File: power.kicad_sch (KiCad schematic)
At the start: 33 parts, among them U5 TI LMR54410DBV, U6 INA3221AIRGV

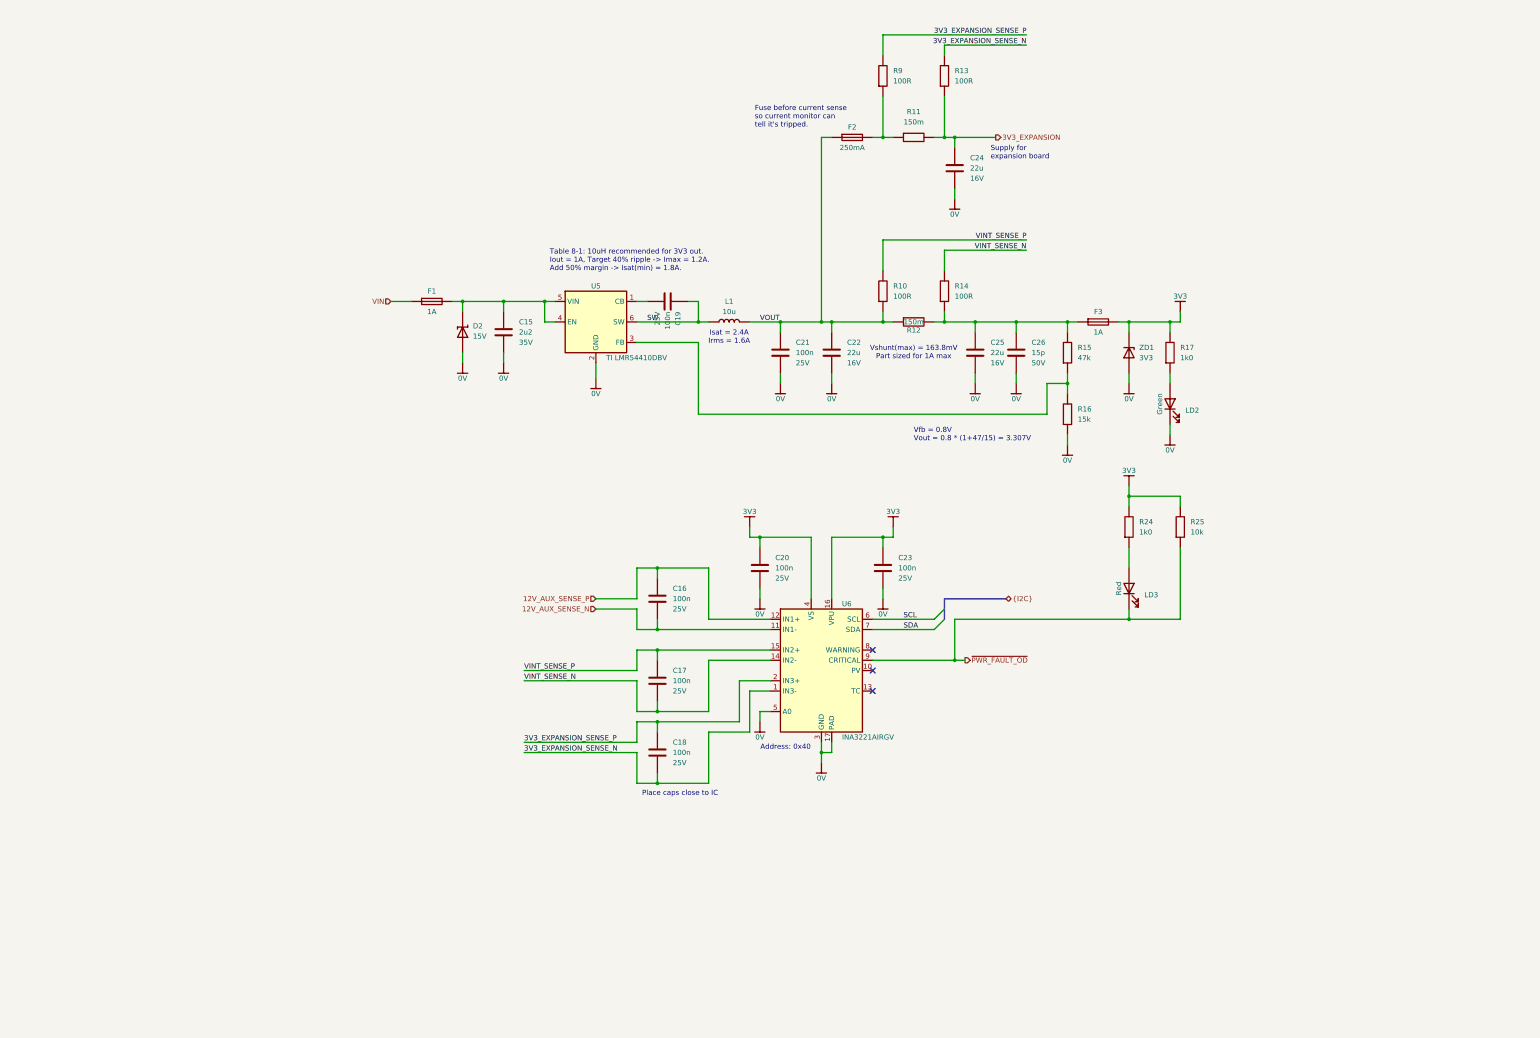
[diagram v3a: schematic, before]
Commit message: added 5v regulator
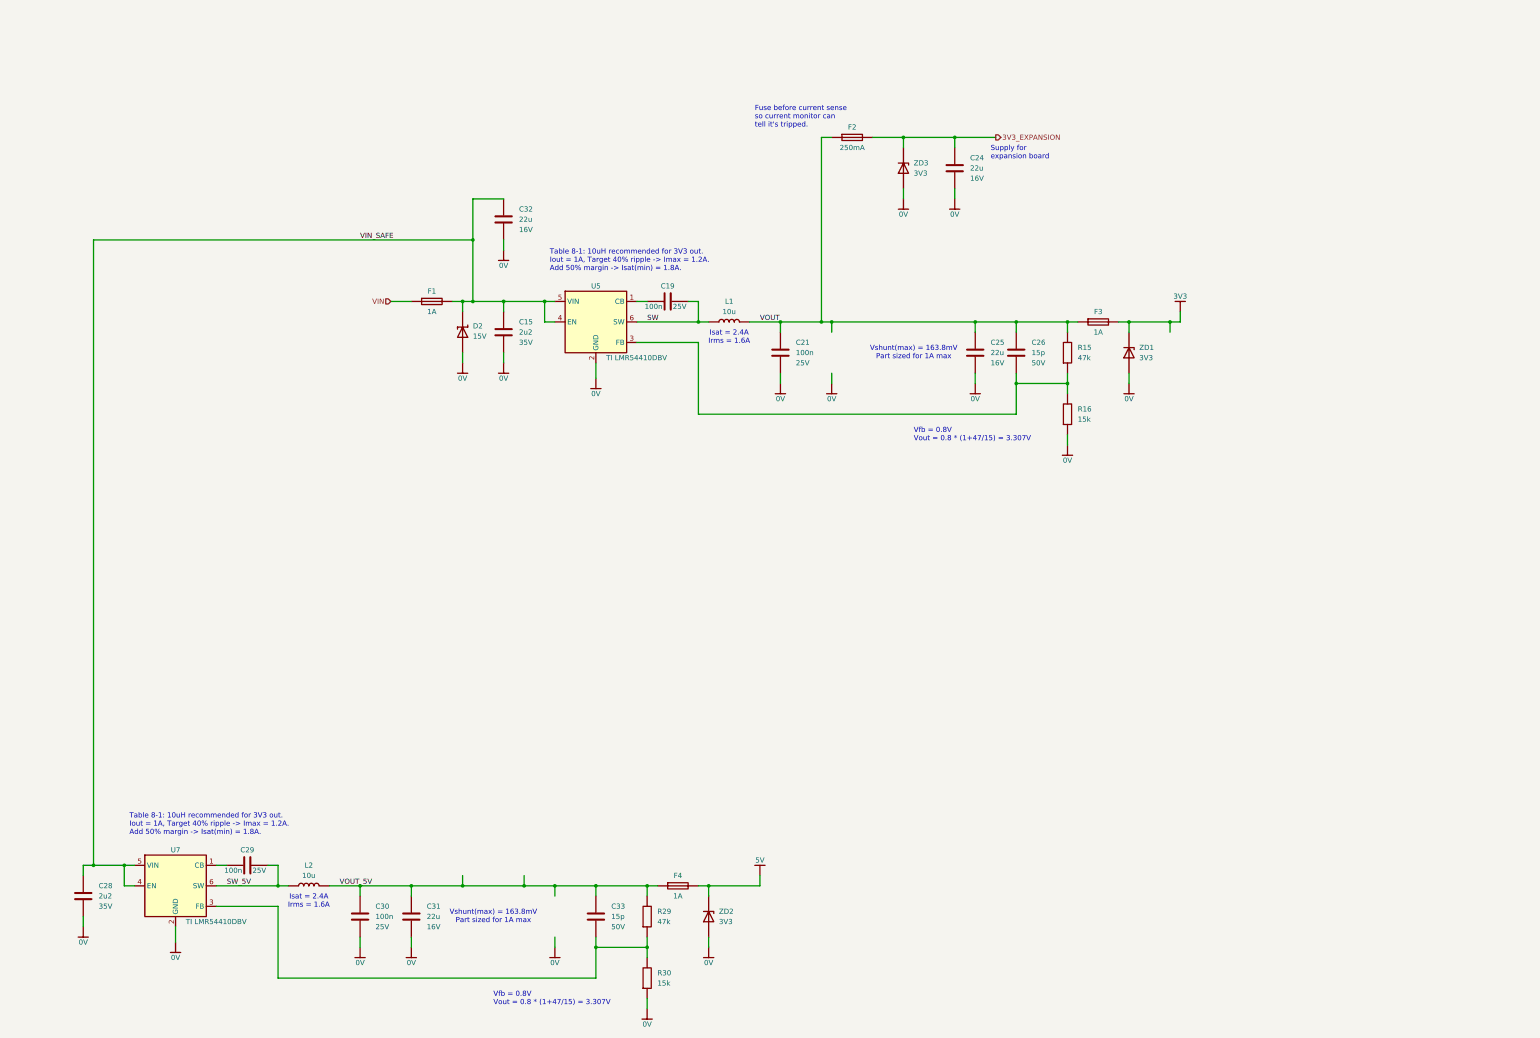
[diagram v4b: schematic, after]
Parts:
- removed C16, C17, C18, C20, C23: 100n, Capacitor_WUT:C_0402_1005Metric, symbol aaa_capacitor_auto_wut:Yageo CC0402KRX7R8BB104
- removed C22: 22u, Capacitor_SMD:C_0603_1608Metric, symbol aaa_capacitor_auto_wut:Murata GRM188R61C226ME01
- removed LD2: Green, LED_SMD:LED_0603_1608Metric, symbol aaa_led_auto_wut:Ekinglux_E6C0603VGAC1UDA
- removed LD3: Red, LED_SMD:LED_0603_1608Metric, symbol aaa_led_auto_wut:Lite-On_LTST-C193KRKT-5A
- removed R10, R13, R14, R9: 100R, Resistor_WUT:R_0402_1005Metric, symbol aaa_resistor_auto_wut:KOA Speer RK73H1ETTP1000F
- removed R11, R12: 150m, Resistor_SMD:R_0805_2012Metric, symbol resistor_auto_wut:Panasonic ERJ6DSFR15V
- removed R17, R24: 1k0, Resistor_WUT:R_0402_1005Metric, symbol aaa_resistor_auto_wut:KOA Speer RK73H1ETTP1001F
- removed R25: 10k, Resistor_WUT:R_0402_1005Metric, symbol aaa_resistor_auto_wut:KOA Speer RK73H1ETTP1002F
- removed U6: INA3221AIRGV, IC_WUT:Texas_VQFN-16-1EP_RGV0016A, symbol IC_WUT:INA3221AIRGV
- added C28: 2u2, Capacitor_WUT:C_0402_1005Metric, symbol capacitor_auto_wut:Murata GRM155R6YA225KE11
- added C29, C30: 100n, Capacitor_WUT:C_0402_1005Metric, symbol aaa_capacitor_auto_wut:Yageo CC0402KRX7R8BB104
- added C31, C32: 22u, Capacitor_SMD:C_0603_1608Metric, symbol aaa_capacitor_auto_wut:Murata GRM188R61C226ME01
- added C33: 15p, Capacitor_WUT:C_0402_1005Metric, symbol capacitor_auto_wut:Kemet C0402C150G5GACTU
- added F4: 1A, Fuse:Fuse_0603_1608Metric, symbol fuse_auto_wut:Littelfuse 0467001.NR
- added L2: 10u, Inductor_WUT:APV_ANR4030, symbol inductor_auto_wut:APV ANR4030T100M
- added R29: 47k, Resistor_WUT:R_0402_1005Metric, symbol resistor_auto_wut:KOA Speer RK73H1ETTP4702F
- added R30: 15k, Resistor_WUT:R_0402_1005Metric, symbol resistor_auto_wut:KOA Speer RK73H1ETTP1502F
- added U7: TI LMR54410DBV, IC_WUT:SOT-23-6, symbol IC_WUT:TI_LMR54410DBV
- added ZD2, ZD3: 3V3, Diode_SMD:D_SOD-323, symbol tvs_zener_auto_wut:onsemi MM3Z3V3ST1G
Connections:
- net 0V: now also C28.2, C30.2, C31.2, C32.2, R30.2, U7.2 (GND), ZD2.2 (A), ZD3.2 (A); no longer C26.2
- net 3V3_EXPANSION: now also F2.2, ZD3.1 (K)
- net VOUT: now also C25.1, C26.1, F3.1, R15.1
- net VIN_SAFE: now reaches C15.1, D2.1 (K), F1.2, U5.4 (EN), U5.5 (VIN)
- net VIN_SAFE: now also C28.1, C32.1, U7.4 (EN), U7.5 (VIN)
- net at R15.2, R16.1, U5.3 (FB): now also C26.2
- new net: C33.2, R29.2, R30.1, U7.3 (FB)
- new net: C29.2, U7.1 (CB)
- new net 5V: F4.2, ZD2.1 (K)
- new net SW_5V: C29.1, L2.1, U7.6 (SW)
- new net VOUT_5V: C30.1, C31.1, C33.1, F4.1, L2.2, R29.1
- no-connect marks 3 -> 0
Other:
- note removed: "Address: 0x40"
- note removed: "Place caps close to IC"

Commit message: wup
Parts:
- removed C24: 22u, Capacitor_SMD:C_0603_1608Metric, symbol aaa_capacitor_auto_wut:Murata GRM188R61C226ME01
- removed F2: 250mA, Fuse:Fuse_0603_1608Metric, symbol fuse_auto_wut:Littelfuse 0603L025
- removed F4: 1A, Fuse:Fuse_0603_1608Metric, symbol fuse_auto_wut:Littelfuse 0467001.NR
- removed ZD1, ZD2, ZD3: 3V3, Diode_SMD:D_SOD-323, symbol tvs_zener_auto_wut:onsemi MM3Z3V3ST1G
- added C20, C22, C23: 47u, Capacitor_SMD:C_1206_3216Metric, symbol capacitor_auto_wut:TDK C3216X5R1E476M160AC
- added C34: 100n, Capacitor_WUT:C_0402_1005Metric, symbol aaa_capacitor_auto_wut:Yageo CC0402KRX7R8BB104
- added D13, D14: 5V, Diode_SMD:D_SOD-523, symbol aaa_tvs_zener_auto_wut:hongjiacheng H5VND5U
- added F2: 1A, Fuse:Fuse_0603_1608Metric, symbol fuse_auto_wut:Littelfuse 0467001.NR
- added R10, R11: 10k, Resistor_WUT:R_0402_1005Metric, symbol aaa_resistor_auto_wut:KOA Speer RK73H1ETTP1002F
- added R9: 47k, Resistor_WUT:R_0402_1005Metric, symbol resistor_auto_wut:KOA Speer RK73H1ETTP4702F
- added U6: TI TPS2553DBV, IC_WUT:SOT-23-6, symbol IC_WUT:TPS2553DBV
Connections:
- net SW is gone; now on net SW_5V: C19.1, L1.1, U5.6 (SW)
- net 0V: now also C20.2, C22.2, C23.2, C34.2, D13.2 (A), D14.2 (A), R10.2, R9.2, U6.2 (GND)
- net 3V3: now also D13.1 (K), R11.1
- net 5V: now also C34.1, D14.1 (K), F2.2, U6.1 (IN)
- net SW_5V: no longer C29.1, L2.1, U7.6 (SW)
- net VOUT_5V: now also C21.1, C25.1, C26.1, L1.2, R15.1, F2.1; no longer C30.1, C31.1, C33.1, L2.2, R29.1
- removed net VOUT: C21.1, C25.1, C26.1, F3.1, L1.2, R15.1
- new net: R9.1, U6.5 (ILIM)
- new net 5V_VBUS: C20.1, C22.1, C23.1, U6.6 (OUT)
- new net SW_3V3: C29.1, L2.1, U7.6 (SW)
- new net VBUS_EN: R10.1, U6.3 (EN)
- new net VOUT_3V3: C30.1, C31.1, C33.1, F3.1, L2.2, R29.1
- new net ~{VBUS_FAULT}: R11.2, U6.4 (~{FAULT})
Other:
- note added: "3V3 1A"
- note added: "5V 500mA"
- note added: "Datasheet recommends 15uH but that's an extra BOM item so trying 10uH for now and may just add more output capacitance."
- note added: "GRM21BR61E226ME44L"
- note added: "IOSnom(mA) = 23950V / (R_ILIM (kohm) ^ 0.977) = 556mA (Eqn 1)"
- note added: "Iout = 0.5A, Target 40% ripple -> Imax = 0.6A. Add 50% margin -> Isat(min) = 0.9A."
- note added: "Most of an attempt at 120uF required for USB downstream"
- note added: "USB Load Switch"
- note added: "Vih = 1.1V so MCU IO is fine"
- note removed: "Fuse before current sense so current monitor can tell it's tripped."
- note removed: "Supply for expansion board"
- note removed: "Vshunt(max) = 163.8mV Part sized for 1A max"
- moved on the sheet: C15, C19, C21, C25, C26, C28, C29, C30, C31, C33, D2, F1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

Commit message: did a few little bits on layout
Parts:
- removed C20, C22, C23: 47u, Capacitor_SMD:C_1206_3216Metric, symbol capacitor_auto_wut:TDK C3216X5R1E476M160AC
- added C35, C36, C37, C38: 22u, Capacitor_SMD:C_0603_1608Metric, symbol aaa_capacitor_auto_wut:Murata GRM188R61C226ME01
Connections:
- net 0V: now also C35.2, C36.2, C37.2, C38.2
- net 5V_VBUS: now also C35.1, C36.1, C37.1, C38.1
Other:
- note added: "TODO Feedback resistors"
- note removed: "GRM21BR61E226ME44L"

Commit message: more progress
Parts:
- removed C32: 22u, Capacitor_SMD:C_0603_1608Metric, symbol aaa_capacitor_auto_wut:Murata GRM188R61C226ME01
- added R32, R33, R34, R4: 1k0, Resistor_WUT:R_0402_1005Metric, symbol aaa_resistor_auto_wut:KOA Speer RK73H1ETTP1001F
- renumbered C34 to C30, C28 to C31, C15 to C32, C29 to C33, C19 to C34, C36 to C35, C35 to C36, C30 to C37, C21 to C38, C37 to C39, C31 to C40, C25 to C41, C38 to C42, C33 to C43, C26 to C44, D2 to D11, D13 to D12, D14 to D13, F1 to F2, F2 to F4, L2 to L1, L1 to L2, R10 to R16, R9 to R17, R11 to R18, R29 to R19, R30 to R20, R15 to R21, R16 to R22, U7 to U5, U5 to U6, U6 to U7
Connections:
- net 0V: now also R33.2, R34.2
- net 3V3: now also R4.1
- net 5V: now also R32.1
- new net: R32.2, R34.1
- new net: R33.1, R4.2
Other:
- note added: "TODO Replace with 0402 LEDs"
- note added: "TODO input cap"
